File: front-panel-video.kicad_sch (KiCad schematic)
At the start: 23 parts, among them J5 DisplayPort-Mini_Pulse_E9320-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, U11 TPD4E05U06QDQARQ1, U12 TPD4E05U06QDQARQ1, U13 TPD4E05U06QDQARQ1

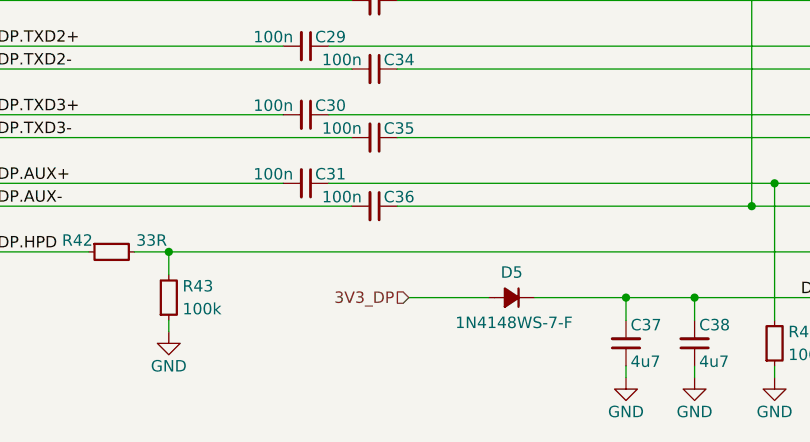
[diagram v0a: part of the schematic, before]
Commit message: [#83363] Adjusted DP PWR connection
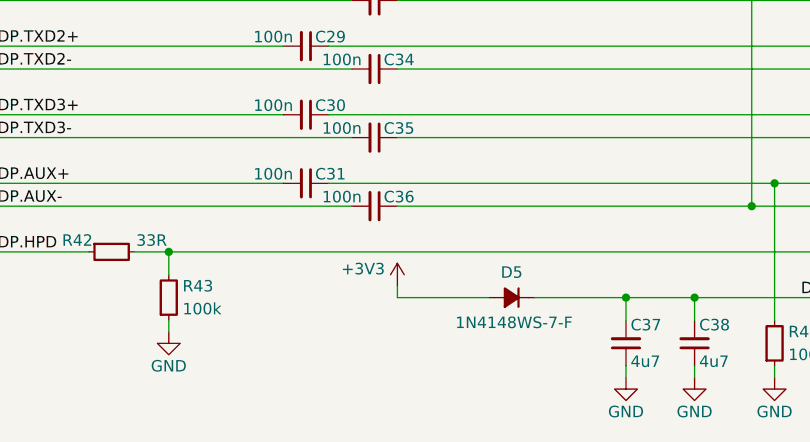
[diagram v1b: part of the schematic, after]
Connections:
- net 3V3_DP renamed +3V3
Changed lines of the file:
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@@
 	(wire
 		(pts
-			(xy 144.78 107.95) (xy 204.47 107.95)
+			(xy 152.4 151.13) (xy 162.56 151.13)
 		)
 		(stroke
@@
 	(wire
 		(pts
-			(xy 152.4 110.49) (xy 204.47 110.49)
+			(xy 144.78 107.95) (xy 204.47 107.95)
 		)
 		(stroke
@@
 	(wire
 		(pts
-			(xy 153.67 151.13) (xy 162.56 151.13)
+			(xy 152.4 110.49) (xy 204.47 110.49)
 		)
 		(stroke
@@
 	(wire
 		(pts
+			(xy 152.4 149.86) (xy 152.4 151.13)
+		)
+		(stroke
+			(width 0)
+			(type default)
+		)
+	)
+	(wire
+		(pts
 			(xy 191.77 99.06) (xy 191.77 100.33)
 		)
@@
 		)
 	)
-	(hierarchical_label "3V3_DP"
-		(shape input)
-		(at 153.67 151.13 180)
-		(effects
-			(font
-				(size 1.27 1.27)
-			)
-			(justify right)
-		)
-	)
 	(symbol
 		(lib_id "antmicroCapacitors0402:C_100n_0402")
@@
 					(unit 1)
 				)
+			)
+		)
+	)
+	(symbol
+		(lib_id "antmicropower:+3V3")
+		(at 152.4 149.86 0)
+		(unit 1)
+		(exclude_from_sim no)
+		(in_bom yes)
+		(on_board yes)
+		(dnp no)
+		(property "Reference" "#PWR0199"
+			(at 167.64 149.86 0)
+			(effects
+				(font
+					(size 1.27 1.27)
+					(thickness 0.15)
+				)
+				(justify left bottom)
+				(hide yes)
+			)
+		)
+		(property "Value" "+3V3"
+			(at 148.59 147.955 0)
+			(effects
+				(font
+					(size 1.27 1.27)
+					(thickness 0.15)
+				)
+			)
+		)
+		(property "Footprint" ""
+			(at 167.64 157.48 0)
+			(effects
+				(font
+					(size 1.27 1.27)
+					(thickness 0.15)
+				)
+				(justify left bottom)
+				(hide yes)
+			)
+		)
+		(property "Datasheet" ""
+			(at 167.64 160.02 0)
+			(effects
+				(font
+					(size 1.27 1.27)
+					(thickness 0.15)
+				)
+				(justify left bottom)
+				(hide yes)
+			)
+		)
+		(property "Description" ""
+			(at 152.4 149.86 0)
+			(effects
+				(font
+					(size 1.27 1.27)
+				)
+				(hide yes)
+			)
+		)
+		(property "Author" "Antmicro"
+			(at 167.64 152.4 0)
+			(effects
+				(font
+					(size 1.27 1.27)
+					(thickness 0.15)
+				)
+				(justify left bottom)
+				(hide yes)
+			)
+		)
+		(property "License" "Apache-2.0"
+			(at 167.64 154.94 0)
+			(effects
+				(font
+					(size 1.27 1.27)
+					(thickness 0.15)
+				)
+				(justify left bottom)
+				(hide yes)
+			)
+		)
+		(pin "1"
+		)
+		(instances
+			(project ""
+				(path "/5f636c45-3c15-4731-8931-4625e0dab7e4/32de8c9e-be2b-4d78-9d5d-f4e694f2d2e7"
+					(reference "#PWR0199")
+					(unit 1)
+				)

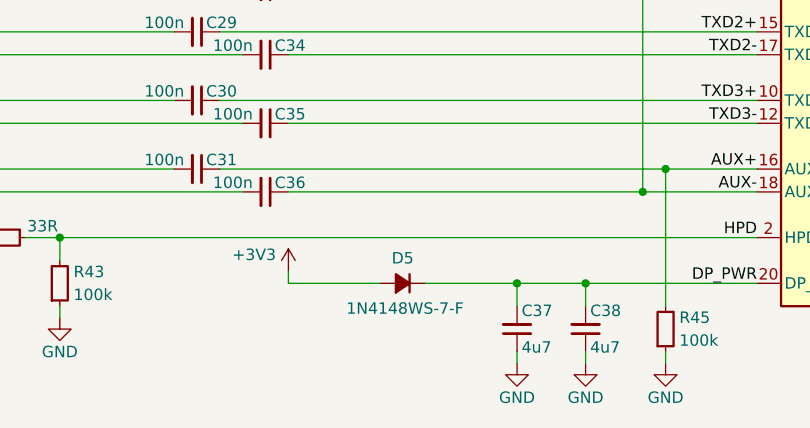
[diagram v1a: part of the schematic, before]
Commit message: [#83336] Small front panel interface fixes
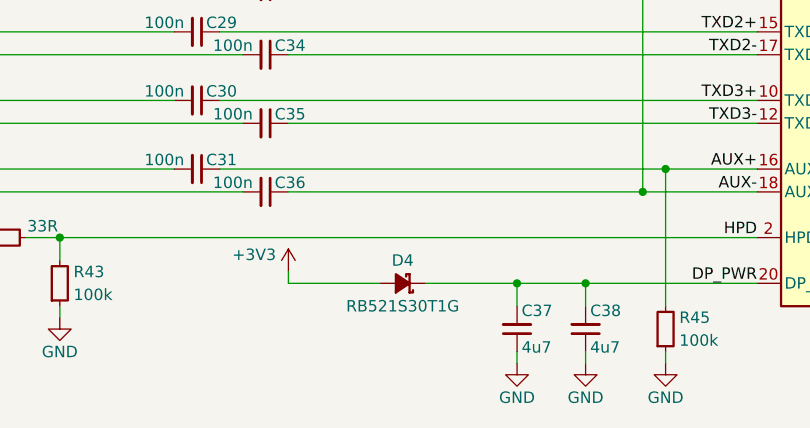
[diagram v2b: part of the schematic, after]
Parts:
- removed D5: 1N4148WS-7-F, antmicro-footprints:D_SOD-323, symbol antmicroDiodesRectifiersSingle:1N4148WS-7-F
- added D4: RB521S30T1G, antmicro-footprints:SOD-523, symbol antmicroDiodesRectifiersSingle:RB521S30T1G
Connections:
- net +3V3: now also D4.2 (A)
- net DP_PWR: now also D4.1 (C)
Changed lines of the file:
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@@
+	)
+	(symbol
+		(lib_id "antmicroDiodesRectifiersSingle:RB521S30T1G")
+		(at 167.64 151.13 180)
+		(unit 1)
+		(exclude_from_sim no)
+		(in_bom yes)
+		(on_board yes)
+		(dnp no)
+		(property "Reference" "D4"
+			(at 165.1 148.59 0)
+			(effects
+				(font
+					(size 1.27 1.27)
+					(thickness 0.15)
+				)
+			)
+		)
+		(property "Value" "RB521S30T1G"
+			(at 144.78 135.89 0)
+			(effects
+				(font
+					(size 1.27 1.27)
+					(thickness 0.15)
+				)
+				(justify left bottom)
+				(hide yes)
+			)
+		)
+		(property "Footprint" "antmicro-footprints:SOD-523"
+			(at 144.78 140.97 0)
+			(effects
+				(font
+					(size 1.27 1.27)
+					(thickness 0.15)
+				)
+				(justify left bottom)
+				(hide yes)
+			)
+		)
+		(property "Datasheet" "https://www.onsemi.com/pdf/datasheet/rb521s30t1-d.pdf"
+			(at 144.78 138.43 0)
+			(effects
+				(font
+					(size 1.27 1.27)
+					(thickness 0.15)
+				)
+				(justify left bottom)
+				(hide yes)
+			)
+		)
+		(property "Description" "Small Signal Schottky Diode, Single, 30 V, 200 mA, 500 mV, 1 A, 125 °C"
+			(at 167.64 151.13 0)
+			(effects
+				(font
+					(size 1.27 1.27)
+				)
+				(hide yes)
+			)
+		)
+		(property "MPN" "RB521S30T1G"
+			(at 165.1 153.67 0)
+			(effects
+				(font
+					(size 1.27 1.27)
+					(thickness 0.15)
+				)
+			)
+		)
+		(property "Manufacturer" "ON Semiconductor"
+			(at 144.78 133.35 0)
+			(effects
+				(font
+					(size 1.27 1.27)
+					(thickness 0.15)
+				)
+				(justify left bottom)
+				(hide yes)
+			)
+		)
+		(property "Author" "Antmicro"
+			(at 144.78 130.81 0)
+			(effects
+				(font
+					(size 1.27 1.27)
+					(thickness 0.15)
+				)
+				(justify left bottom)
+				(hide yes)
+			)
+		)
+		(property "License" "Apache-2.0"
+			(at 144.78 128.27 0)
+			(effects
+				(font
+					(size 1.27 1.27)
+					(thickness 0.15)
+				)
+				(justify left bottom)
+				(hide yes)
+			)
+		)
+		(pin "1"
+		)
+		(pin "2"
+		)
+		(instances
+			(project ""
+				(path "/5f636c45-3c15-4731-8931-4625e0dab7e4/32de8c9e-be2b-4d78-9d5d-f4e694f2d2e7"
+					(reference "D4")
+					(unit 1)
+				)
+			)
+		)
 	)
 	(symbol
@@
 					(unit 1)
 				)
-			)
-		)
-	)
-	(symbol
-		(lib_id "antmicroDiodesRectifiersSingle:1N4148WS-7-F")
-		(at 167.64 151.13 180)
-		(unit 1)
-		(exclude_from_sim no)
-		(in_bom yes)
-		(on_board yes)
-		(dnp no)
-		(property "Reference" "D5"
-			(at 165.1 148.336 0)
-			(effects
-				(font
-					(size 1.27 1.27)
-					(thickness 0.15)
-				)
-			)
-		)
-		(property "Value" "1N4148WS-7-F"
-			(at 146.05 140.97 0)
-			(effects
-				(font
-					(size 1.27 1.27)
-					(thickness 0.15)
-				)
-				(justify left bottom)
-				(hide yes)
-			)
-		)
-		(property "Footprint" "antmicro-footprints:D_SOD-323"
-			(at 146.05 138.43 0)
-			(effects
-				(font
-					(size 1.27 1.27)
-					(thickness 0.15)
-				)
-				(justify left bottom)
-				(hide yes)
-			)
-		)
-		(property "Datasheet" "https://www.diodes.com/assets/Datasheets/ds30097.pdf"
-			(at 146.05 135.89 0)
-			(effects
-				(font
-					(size 1.27 1.27)
-					(thickness 0.15)
-				)
-				(justify left bottom)
-				(hide yes)
-			)
-		)
-		(property "Description" "Fast Switching Diode, Single, 75 V, 300 mA, 1.25 V, 4 ns, 2 A"
-			(at 167.64 151.13 0)
-			(effects
-				(font
-					(size 1.27 1.27)
-				)
-				(hide yes)
-			)
-		)
-		(property "MPN" "1N4148WS-7-F"
-			(at 165.354 153.924 0)
-			(effects
-				(font
-					(size 1.27 1.27)
-					(thickness 0.15)
-				)
-			)
-		)
-		(property "Manufacturer" "Diodes Incorporated"
-			(at 146.05 133.35 0)
-			(effects
-				(font
-					(size 1.27 1.27)
-					(thickness 0.15)
-				)
-				(justify left bottom)
-				(hide yes)
-			)
-		)
-		(property "Author" "Antmicro"
-			(at 146.05 130.81 0)
-			(effects
-				(font
-					(size 1.27 1.27)
-					(thickness 0.15)
-				)
-				(justify left bottom)
-				(hide yes)
-			)
-		)
-		(property "License" "Apache-2.0"
-			(at 146.05 128.27 0)
-			(effects
-				(font
-					(size 1.27 1.27)
-					(thickness 0.15)
-				)
-				(justify left bottom)
-				(hide yes)
-			)
-		)
-		(pin "1"
-		)
-		(pin "2"
-		)
-		(instances
-			(project ""
-				(path "/5f636c45-3c15-4731-8931-4625e0dab7e4/32de8c9e-be2b-4d78-9d5d-f4e694f2d2e7"
-					(reference "D5")
-					(unit 1)
-				)

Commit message: [#83609] Reannotate board
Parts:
- renumbered C27 to C82, C28 to C83, C29 to C84, C30 to C85, C31 to C86, C32 to C87, C33 to C88, C34 to C89, C35 to C90, C36 to C91, C37 to C92, C38 to C93, D4 to D11, J5 to J9, R42 to R196, R43 to R197, R44 to R198, R45 to R199, R46 to R200, R47 to R201, U11 to U21, U12 to U22, U13 to U23

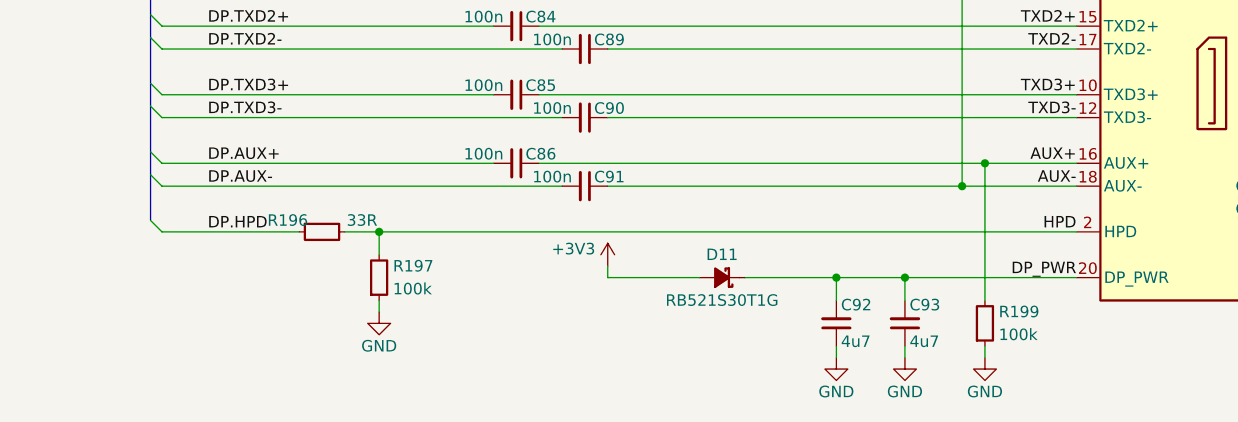
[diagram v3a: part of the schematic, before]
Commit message: [#83736] Fix overlaping text and graphics, fix notes regarding USB-C role
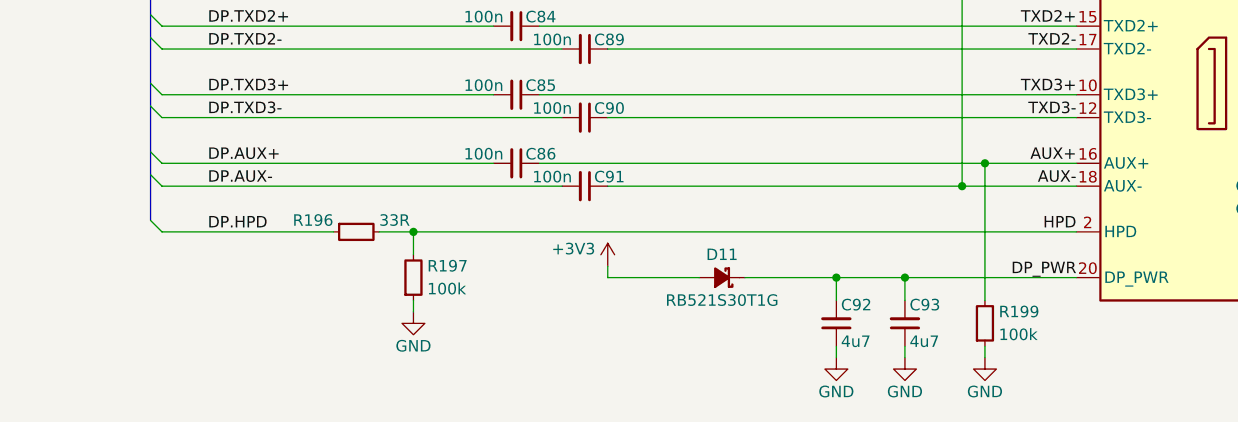
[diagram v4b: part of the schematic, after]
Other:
- moved on the sheet: R196, R197
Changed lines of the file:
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@@
 	)
 	(junction
-		(at 127 146.05)
+		(at 130.81 146.05)
 		(diameter 0)
 		(color 0 0 0 0)
@@
 	(wire
 		(pts
-			(xy 127 146.05) (xy 204.47 146.05)
+			(xy 130.81 146.05) (xy 204.47 146.05)
 		)
 		(stroke
@@
 	(wire
 		(pts
-			(xy 102.87 146.05) (xy 118.11 146.05)
+			(xy 102.87 146.05) (xy 121.92 146.05)
 		)
 		(stroke
@@
 	(wire
 		(pts
-			(xy 123.19 146.05) (xy 127 146.05)
+			(xy 127 146.05) (xy 130.81 146.05)
 		)
 		(stroke
@@
 	(wire
 		(pts
-			(xy 127 146.05) (xy 127 148.59)
+			(xy 130.81 146.05) (xy 130.81 148.59)
 		)
 		(stroke
@@
 	(wire
 		(pts
-			(xy 127 153.67) (xy 127 154.94)
+			(xy 130.81 153.67) (xy 130.81 154.94)
 		)
 		(stroke
@@
 	(symbol
 		(lib_id "antmicropower:GND")
-		(at 127 154.94 0)
+		(at 130.81 154.94 0)
 		(unit 1)
 		(exclude_from_sim no)
@@
 		(dnp no)
 		(property "Reference" "#PWR0177"
-			(at 135.89 157.48 0)
+			(at 139.7 157.48 0)
 			(effects
 				(font
@@
 		)
 		(property "Value" "GND"
-			(at 127 158.75 0)
+			(at 130.81 158.75 0)
 			(effects
 				(font
@@
 		)
 		(property "Footprint" ""
-			(at 135.89 162.56 0)
+			(at 139.7 162.56 0)
 			(effects
 				(font
@@
 		)
 		(property "Datasheet" ""
-			(at 135.89 167.64 0)
+			(at 139.7 167.64 0)
 			(effects
 				(font
@@
 		)
 		(property "Description" ""
-			(at 127 154.94 0)
+			(at 130.81 154.94 0)
 			(effects
 				(font
@@
 		)
 		(property "Author" "Antmicro"
-			(at 135.89 162.56 0)
+			(at 139.7 162.56 0)
 			(effects
 				(font
@@
 		)
 		(property "License" "Apache-2.0"
-			(at 135.89 165.1 0)
+			(at 139.7 165.1 0)
 			(effects
 				(font
@@
 	(symbol
 		(lib_id "antmicroResistors0402:R_33R_0402")
-		(at 118.11 146.05 0)
+		(at 121.92 146.05 0)
 		(unit 1)
 		(exclude_from_sim no)
@@
 		(dnp no)
 		(property "Reference" "R196"
-			(at 116.84 144.78 0)
+			(at 121.92 144.78 0)
 			(effects
 				(font
@@
 					(thickness 0.15)
 				)
+				(justify right)
 			)
 		)
 		(property "Value" "R_33R_0402"
-			(at 138.43 158.75 0)
+			(at 142.24 158.75 0)
 			(effects
 				(font
@@
 		)
 		(property "Footprint" "antmicro-footprints:R_0402_1005Metric"
-			(at 138.43 161.29 0)
+			(at 142.24 161.29 0)
 			(effects
 				(font
@@
 		)
 		(property "Datasheet" "https://www.bourns.com/docs/product-datasheets/cr.pdf"
-			(at 138.43 163.83 0)
+			(at 142.24 163.83 0)
 			(effects
 				(font
@@
 		)
 		(property "Description" "SMD Chip Resistor, 33 ohm, ± 1%, 62.5 mW, 0402 [1005 Metric], Thick Film, General Purpose"
-			(at 118.11 146.05 0)
+			(at 121.92 146.05 0)
 			(effects
 				(font
@@
 		)
 		(property "MPN" "CR0402-FX-33R0GLF"
-			(at 138.43 166.37 0)
+			(at 142.24 166.37 0)
 			(effects
 				(font
@@
 		)
 		(property "Manufacturer" "Bourns"
-			(at 138.43 168.91 0)
+			(at 142.24 168.91 0)
 			(effects
 				(font
@@
 		)
 		(property "License" "Apache-2.0"
-			(at 138.43 171.45 0)
+			(at 142.24 171.45 0)
 			(effects
 				(font
@@
 		)
 		(property "Author" "Antmicro"
-			(at 138.43 173.99 0)
+			(at 142.24 173.99 0)
 			(effects
 				(font
@@
 		)
 		(property "Val" "33R"
-			(at 125.095 144.78 0)
+			(at 127 144.78 0)
 			(effects
 				(font
@@
 					(thickness 0.15)
 				)
+				(justify left)
 			)
 		)
 		(property "Tolerance" "1%"
-			(at 138.43 156.21 0)
+			(at 142.24 156.21 0)
 			(effects
 				(font
@@
 	(symbol
 		(lib_id "antmicroResistors0402:R_100k_0402")
-		(at 127 153.67 90)
+		(at 130.81 153.67 90)
 		(unit 1)
 		(exclude_from_sim no)
@@
 		(dnp no)
 		(property "Reference" "R197"
-			(at 128.524 149.86 90)
+			(at 132.334 149.86 90)
 			(effects
 				(font
@@
 		)
 		(property "Value" "R_100k_0402"
-			(at 139.7 133.35 0)
+			(at 143.51 133.35 0)
 			(effects
 				(font
@@
 		)
 		(property "Footprint" "antmicro-footprints:R_0402_1005Metric"
-			(at 142.24 133.35 0)
+			(at 146.05 133.35 0)
 			(effects
 				(font
@@
 		)
 		(property "Datasheet" "https://www.bourns.com/docs/product-datasheets/cr.pdf"
-			(at 144.78 133.35 0)
+			(at 148.59 133.35 0)
 			(effects
 				(font
@@
 		)
 		(property "Description" "SMD Chip Resistor, 100 kohm, ± 1%, 62.5 mW, 0402 [1005 Metric], Thick Film, General Purpose"
-			(at 127 153.67 0)
+			(at 130.81 153.67 0)
 			(effects
 				(font
@@
 		)
 		(property "MPN" "CR0402-FX-1003GLF"
-			(at 147.32 133.35 0)
+			(at 151.13 133.35 0)
 			(effects
 				(font
@@
 		)
 		(property "Manufacturer" "Bourns"
-			(at 149.86 133.35 0)
+			(at 153.67 133.35 0)
 			(effects
 				(font
@@
 		)
 		(property "License" "Apache-2.0"
-			(at 152.4 133.35 0)
+			(at 156.21 133.35 0)
 			(effects
 				(font
@@
 		)
 		(property "Author" "Antmicro"
-			(at 154.94 133.35 0)
+			(at 158.75 133.35 0)
 			(effects
 				(font
@@
 		)
 		(property "Val" "100k"
-			(at 128.524 152.4 90)
+			(at 132.334 152.4 90)
 			(effects
 				(font
@@
 		)
 		(property "Tolerance" "1%"
-			(at 137.16 133.35 0)
+			(at 140.97 133.35 0)
 			(effects
 				(font
